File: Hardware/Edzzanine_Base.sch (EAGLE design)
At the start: 39 parts, among them U1 MIC5219 3.3V, U2 FTS31XS-U

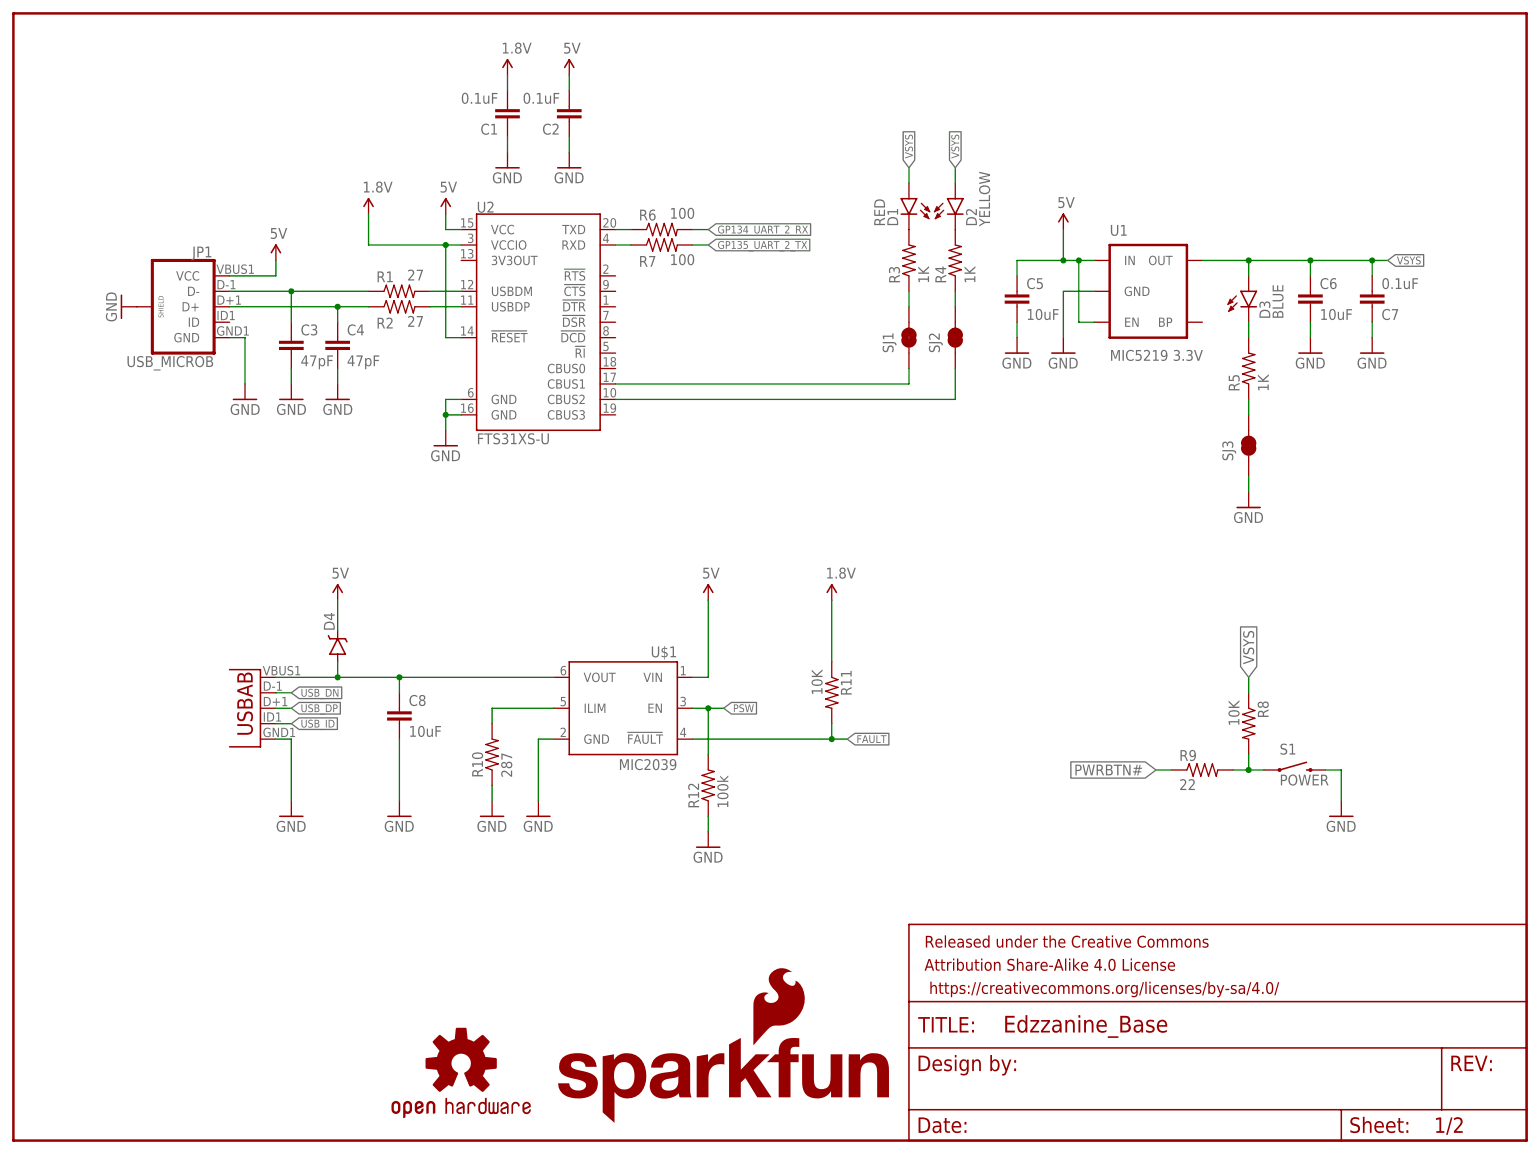
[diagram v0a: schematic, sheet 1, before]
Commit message: changed out power supply for something more powerful. Added fiducials
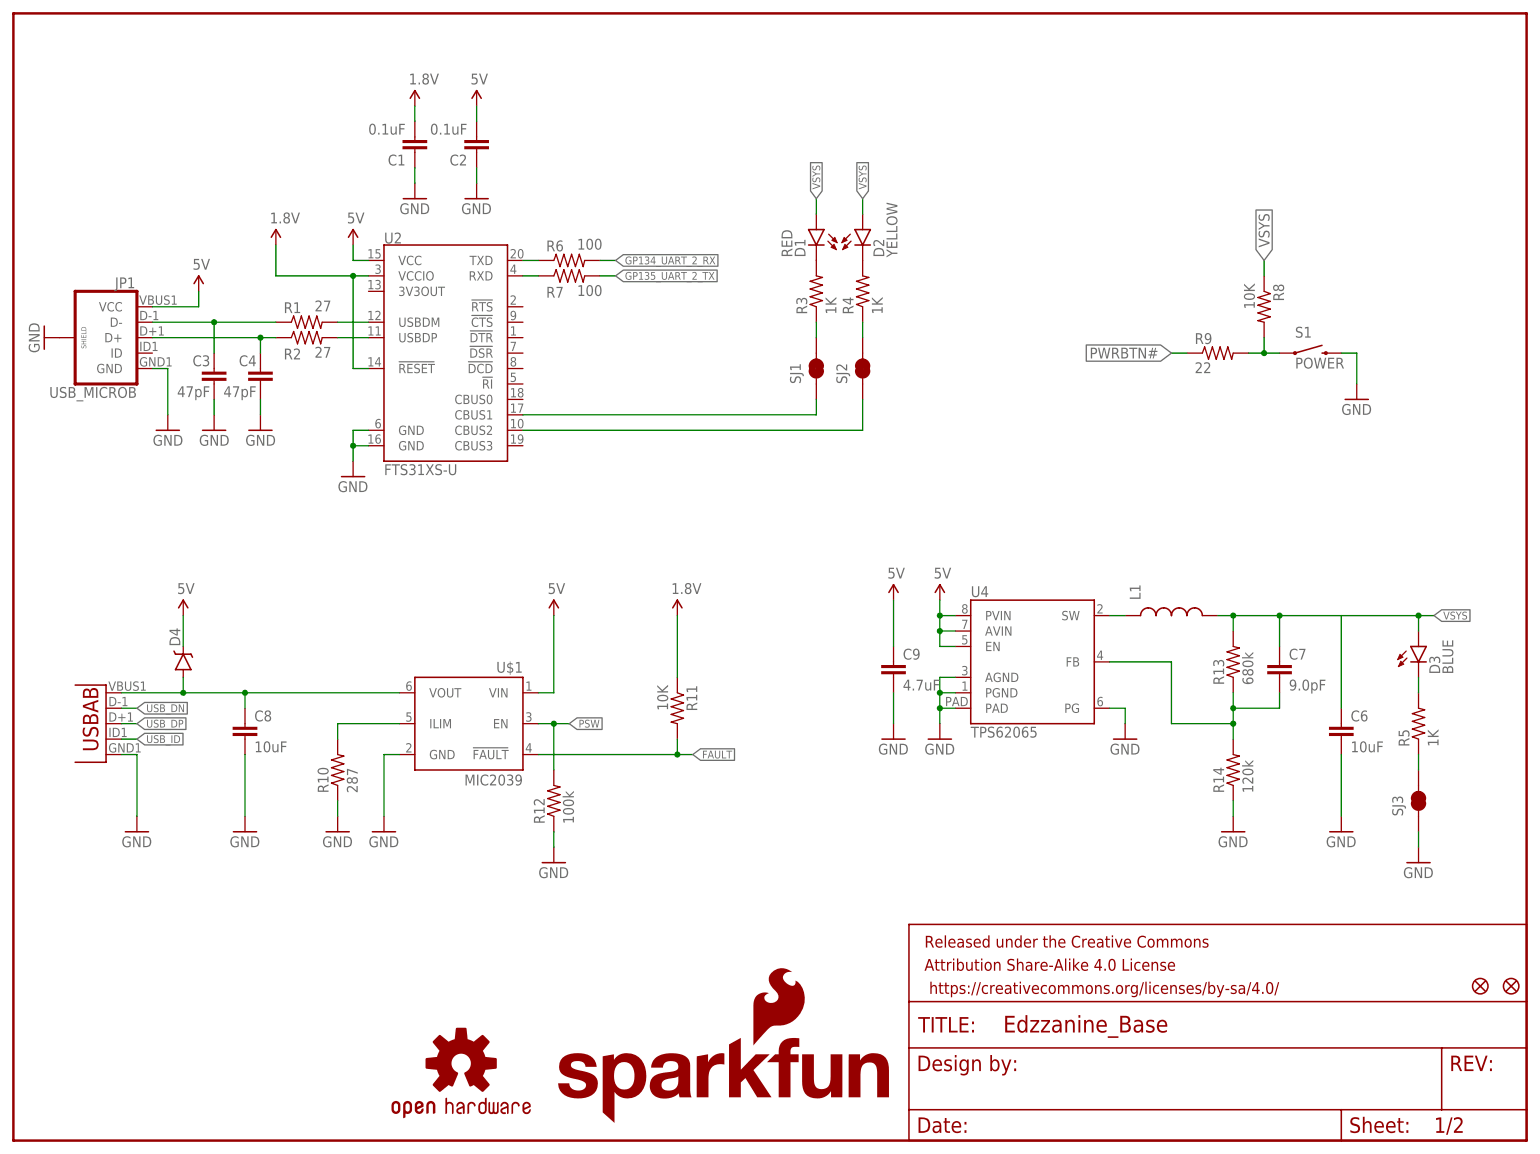
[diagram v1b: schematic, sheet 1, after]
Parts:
- removed C5: 10uF, SparkFun-Capacitors:10UF-6.3V-20%(1206)
- removed U1: MIC5219 3.3V, SparkFun-PowerIC:V_REG_MIC52193.3V
- added C9: 4.7uF, SparkFun-Capacitors:4.7UF-6.3V-10%(0603)0603
- added FID1, FID2: FIDUCIAL1X2, SparkFun-Aesthetics:FIDUCIAL1X2
- added L1: (no value), SparkFun-Passives:INDUCTOR
- added R13: 680k, SparkFun-Resistors:RESISTOR0603
- added R14: 120k, SparkFun-Resistors:RESISTOR0603
- added U4: TPS62065, Testing:TPS62065
- C7: value 0.1uF -> 9.0pF; device SparkFun-Capacitors:0.1UF-25V-5%(0603) -> SparkFun-Capacitors:9.0PF-50V-10%(0603)
- renumbered LOGO2 to LOGO4, LOGO3 to LOGO1
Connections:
- new net N$17: C7.2, R13.1, R14.2, U4.FB
- new net N$19: L1.1, U4.SW
- net 5V: now also C9.1, U4.AVIN, U4.EN, U4.PVIN; no longer C5.1, U1.EN, U1.IN
- net GND: now also C9.2, R14.1, U4.AGND, U4.PAD, U4.PG, U4.PGND; no longer C5.2, C7.1, U1.GND
- net VSYS: now also C7.1, L1.2, R13.2; no longer C7.2, U1.OUT
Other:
- moved on the sheet: C1, C2, C3, C4, C6, C7, C8, D1, D2, D3, D4, JP1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

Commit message: Corrected OTG power issue Corrected name and position added DCIN pin to connector Added DCIN enable circuit corrected dimensions and cleaned up drawings replaced power button with new SMD side shooting button.
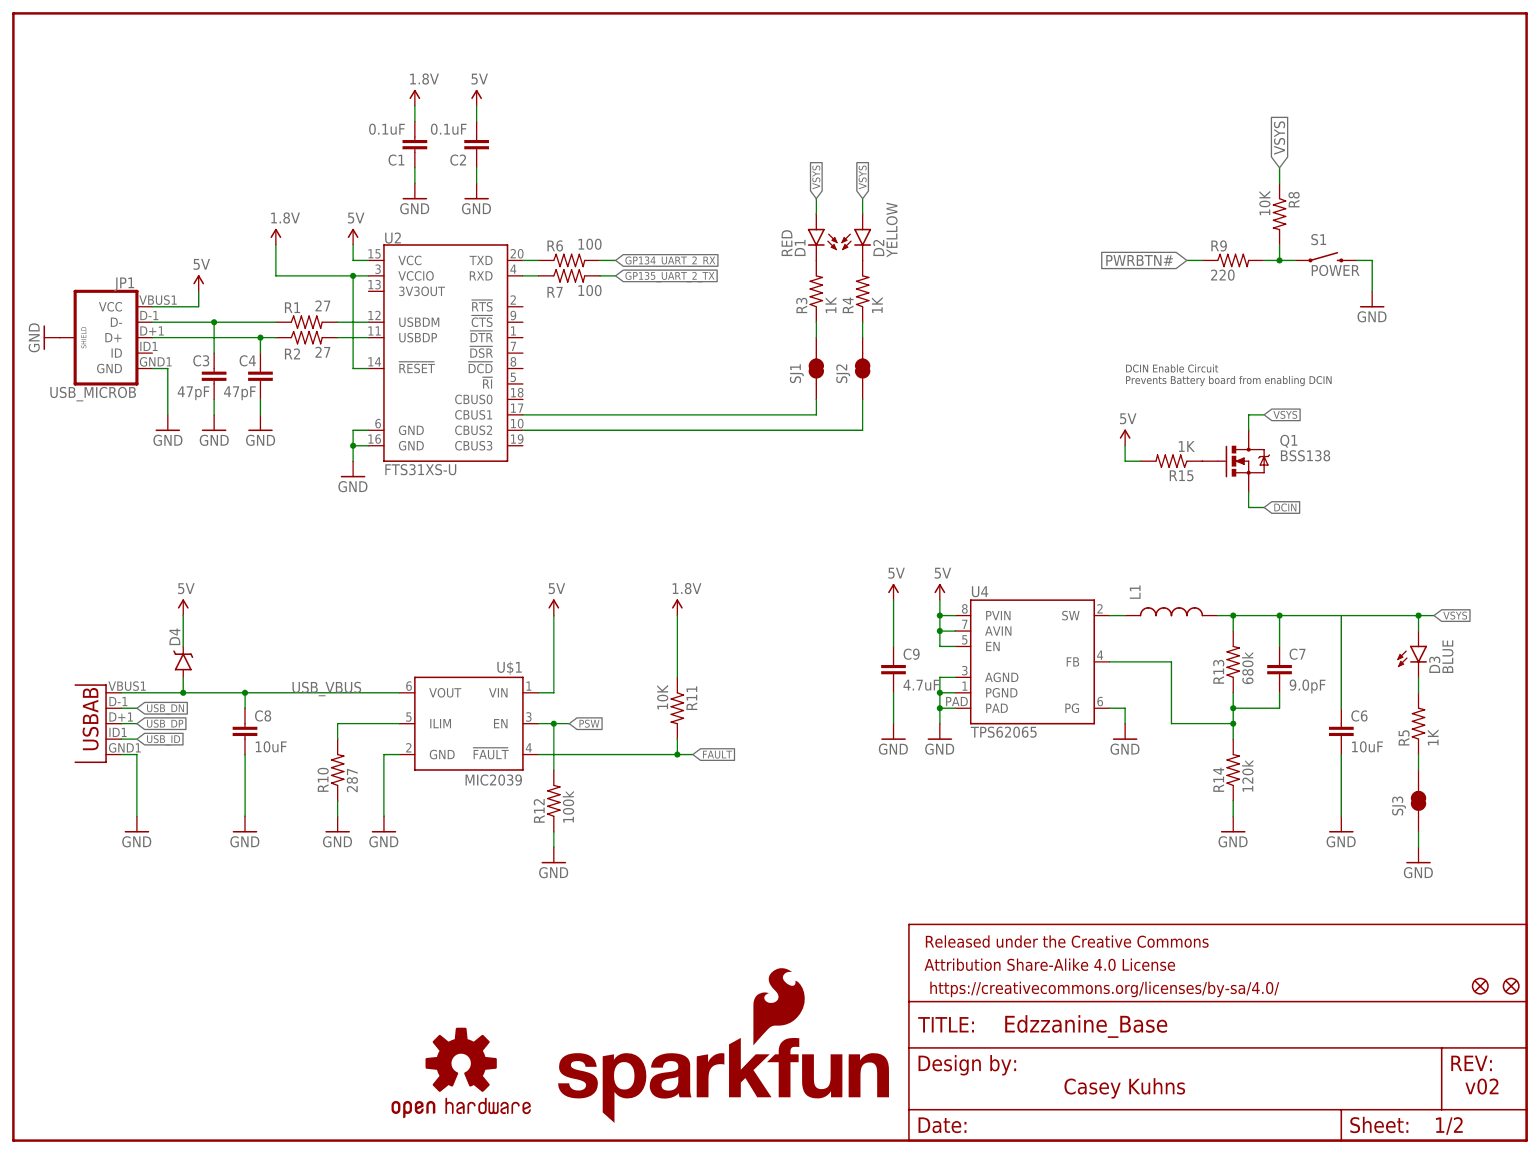
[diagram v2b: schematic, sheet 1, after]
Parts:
- added Q1: BSS138, SparkFun-DiscreteSemi:MOSFET-NCHANNELBSS138
- added R15: 1K, SparkFun-Resistors:1KOHM1/10W1%(0603)
- C1, C2: device SparkFun-Capacitors:0.1UF-25V-5%(0603) -> SparkFun-Capacitors:0.1UF-25V(+80/-20%)(0603)
- R9: value 22 -> 220
- S1: device SparkFun-Electromechanical:SWITCH-MOMENTARY-2-SMD-1101NE -> SparkFun-Electromechanical:SWITCH-MOMENTARY-2TACTILE-SWITCH-SMD-RIGHT-ANGLE
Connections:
- new net DCIN: E1.DCIN, Q1.S, U$3.DCIN
- net 5V: now also R15.2
- net N$18: now also Q1.G, R15.1; no longer C8.1, D4.A, U$1.VOUT, U3.VBUS
- net USB_VBUS: now also C8.1, D4.A, U$1.VOUT, U3.VBUS
- net VSYS: now also Q1.D
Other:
- note added: "Casey Kuhns"
- note added: "DCIN Enable Circuit Prevents Battery board from enabling DCIN"
- note added: "v02"
- moved on the sheet: R8, R9, S1
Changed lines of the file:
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@@
 <part name="GND5" library="SparkFun-Aesthetics" deviceset="GND" device=""/>
 <part name="U2" library="SparkFun-DigitalIC" deviceset="FT231X" device="S" value="FTS31XS-U"/>
-<part name="C1" library="SparkFun-Capacitors" deviceset="0.1UF-25V-5%(0603)" device="" value="0.1uF"/>
-<part name="C2" library="SparkFun-Capacitors" deviceset="0.1UF-25V-5%(0603)" device="" value="0.1uF"/>
+<part name="C1" library="SparkFun-Capacitors" deviceset="0.1UF-25V(+80/-20%)(0603)" device="" value="0.1uF"/>
+<part name="C2" library="SparkFun-Capacitors" deviceset="0.1UF-25V(+80/-20%)(0603)" device="" value="0.1uF"/>
 <part name="GND2" library="SparkFun-Aesthetics" deviceset="GND" device=""/>
 <part name="GND6" library="SparkFun-Aesthetics" deviceset="GND" device=""/>
@@
 <part name="R6" library="SparkFun-Resistors" deviceset="100OHM1/10W1%(0603)" device="" value="100"/>
 <part name="R7" library="SparkFun-Resistors" deviceset="100OHM1/10W1%(0603)" device="" value="100"/>
-<part name="S1" library="SparkFun-Electromechanical" deviceset="SWITCH-MOMENTARY-2" device="-SMD-1101NE" value="POWER"/>
+<part name="S1" library="SparkFun-Electromechanical" deviceset="SWITCH-MOMENTARY-2" device="TACTILE-SWITCH-SMD-RIGHT-ANGLE" value="POWER"/>
 <part name="R8" library="SparkFun-Resistors" deviceset="10KOHM1/10W1%(0603)" device="0603" value="10K"/>
-<part name="R9" library="SparkFun-Resistors" deviceset="22OHM1/10W1%(0603)" device="" value="22"/>
+<part name="R9" library="SparkFun-Resistors" deviceset="22OHM1/10W1%(0603)" device="" value="220"/>
 <part name="GND15" library="SparkFun-Aesthetics" deviceset="GND" device=""/>
 <part name="U3" library="SparkFun-Connectors" deviceset="USB-AB" device="CONN-11794"/>
@@
 <part name="FID1" library="SparkFun-Aesthetics" deviceset="FIDUCIAL" device="1X2"/>
 <part name="FID2" library="SparkFun-Aesthetics" deviceset="FIDUCIAL" device="1X2"/>
+<part name="Q1" library="SparkFun-DiscreteSemi" deviceset="MOSFET-NCHANNEL" device="BSS138" value="BSS138"/>
+<part name="R15" library="SparkFun-Resistors" deviceset="1KOHM1/10W1%(0603)" device="" value="1K"/>
+<part name="SUPPLY7" library="SparkFun-Aesthetics" deviceset="5V" device=""/>
 </parts>
 <sheets>
 <sheet>
 <plain>
+<text x="182.88" y="124.46" size="1.27" layer="97">DCIN Enable Circuit
+Prevents Battery board from enabling DCIN</text>
+<text x="172.72" y="7.62" size="2.54" layer="94">Casey Kuhns</text>
+<text x="238.76" y="7.62" size="2.54" layer="94">v02</text>
 </plain>
 <instances>
@@
 <attribute name="VALUE" x="92.71" y="138.938" size="1.778" layer="96"/>
 </instance>
-<instance part="S1" gate="G$1" x="213.36" y="129.54"/>
-<instance part="R8" gate="G$1" x="205.74" y="137.16" rot="R270"/>
-<instance part="R9" gate="G$1" x="198.12" y="129.54"/>
-<instance part="GND15" gate="1" x="220.98" y="121.92"/>
+<instance part="S1" gate="G$1" x="215.9" y="144.78"/>
+<instance part="R8" gate="G$1" x="208.28" y="152.4" rot="R270"/>
+<instance part="R9" gate="G$1" x="200.66" y="144.78"/>
+<instance part="GND15" gate="1" x="223.52" y="137.16"/>
 <instance part="U3" gate="G$1" x="12.7" y="68.58" rot="R180"/>
 <instance part="GND16" gate="1" x="20.32" y="50.8"/>
@@
 <instance part="FID1" gate="G$1" x="246.38" y="25.4"/>
 <instance part="FID2" gate="G$1" x="241.3" y="25.4"/>
+<instance part="Q1" gate="G$1" x="203.2" y="111.76"/>
+<instance part="R15" gate="G$1" x="190.5" y="111.76" rot="R180"/>
+<instance part="SUPPLY7" gate="G$1" x="182.88" y="114.3"/>
 </instances>
 <busses>
@@
 <segment>
 <pinref part="S1" gate="G$1" pin="2"/>
-<wire x1="218.44" y1="129.54" x2="220.98" y2="129.54" width="0.1524" layer="91"/>
-<wire x1="220.98" y1="129.54" x2="220.98" y2="124.46" width="0.1524" layer="91"/>
+<wire x1="220.98" y1="144.78" x2="223.52" y2="144.78" width="0.1524" layer="91"/>
+<wire x1="223.52" y1="144.78" x2="223.52" y2="139.7" width="0.1524" layer="91"/>
 <pinref part="GND15" gate="1" pin="GND"/>
 </segment>
@@
 <pinref part="SUPPLY11" gate="G$1" pin="5V"/>
 <pinref part="C9" gate="G$1" pin="1"/>
+</segment>
+<segment>
+<pinref part="R15" gate="G$1" pin="2"/>
+<wire x1="182.88" y1="111.76" x2="185.42" y2="111.76" width="0.1524" layer="91"/>
+<pinref part="SUPPLY7" gate="G$1" pin="5V"/>
+<wire x1="182.88" y1="111.76" x2="182.88" y2="114.3" width="0.1524" layer="91"/>
 </segment>
 </net>
@@
 </segment>
 <segment>
-<wire x1="205.74" y1="142.24" x2="205.74" y2="144.78" width="0.1524" layer="91"/>
+<wire x1="208.28" y1="157.48" x2="208.28" y2="160.02" width="0.1524" layer="91"/>
 <pinref part="R8" gate="G$1" pin="1"/>
-<label x="205.74" y="144.78" size="1.778" layer="95" rot="R90" xref="yes"/>
+<label x="208.28" y="160.02" size="1.778" layer="95" rot="R90" xref="yes"/>
+</segment>
+<segment>
+<pinref part="Q1" gate="G$1" pin="D"/>
+<wire x1="203.2" y1="116.84" x2="203.2" y2="119.38" width="0.1524" layer="91"/>
+<wire x1="203.2" y1="119.38" x2="205.74" y2="119.38" width="0.1524" layer="91"/>
+<label x="205.74" y="119.38" size="1.27" layer="95" xref="yes"/>
 </segment>
 </net>
@@
 <pinref part="R9" gate="G$1" pin="2"/>
 <pinref part="R8" gate="G$1" pin="2"/>
-<wire x1="203.2" y1="129.54" x2="205.74" y2="129.54" width="0.1524" layer="91"/>
-<wire x1="205.74" y1="129.54" x2="205.74" y2="132.08" width="0.1524" layer="91"/>
+<wire x1="205.74" y1="144.78" x2="208.28" y2="144.78" width="0.1524" layer="91"/>
+<wire x1="208.28" y1="144.78" x2="208.28" y2="147.32" width="0.1524" layer="91"/>
 <pinref part="S1" gate="G$1" pin="1"/>
-<wire x1="205.74" y1="129.54" x2="208.28" y2="129.54" width="0.1524" layer="91"/>
-<junction x="205.74" y="129.54"/>
+<wire x1="208.28" y1="144.78" x2="210.82" y2="144.78" width="0.1524" layer="91"/>
+<junction x="208.28" y="144.78"/>
 </segment>
 </net>
@@
 <segment>
 <pinref part="R9" gate="G$1" pin="1"/>
-<wire x1="193.04" y1="129.54" x2="190.5" y2="129.54" width="0.1524" layer="91"/>
-<label x="190.5" y="129.54" size="1.778" layer="95" rot="R180" xref="yes"/>
+<wire x1="195.58" y1="144.78" x2="193.04" y2="144.78" width="0.1524" layer="91"/>
+<label x="193.04" y="144.78" size="1.778" layer="95" rot="R180" xref="yes"/>
 </segment>
 </net>
@@
 </segment>
 </net>
-<net name="N$18" class="0">
+<net name="USB_VBUS" class="0">
 <segment>
 <pinref part="U3" gate="G$1" pin="VBUS"/>
@@
 <wire x1="38.1" y1="73.66" x2="63.5" y2="73.66" width="0.1524" layer="91"/>
 <junction x="38.1" y="73.66"/>
+<label x="45.72" y="73.66" size="1.778" layer="95"/>
 </segment>
 </net>
@@
 <pinref part="L1" gate="G$1" pin="1"/>
 <wire x1="182.88" y1="86.36" x2="180.34" y2="86.36" width="0.1524" layer="91"/>
+</segment>
+</net>
+<net name="DCIN" class="0">
+<segment>
+<wire x1="203.2" y1="104.14" x2="205.74" y2="104.14" width="0.1524" layer="91"/>
+<label x="205.74" y="104.14" size="1.27" layer="95" xref="yes"/>
+<pinref part="Q1" gate="G$1" pin="S"/>
+<wire x1="203.2" y1="104.14" x2="203.2" y2="106.68" width="0.1524" layer="91"/>
+</segment>
+</net>
+<net name="N$18" class="0">
+<segment>
+<pinref part="Q1" gate="G$1" pin="G"/>
+<pinref part="R15" gate="G$1" pin="1"/>
 </segment>
 </net>
@@
 </segment>
 </net>
+<net name="DCIN" class="0">
+<segment>
+<pinref part="U$3" gate="G$1" pin="DCIN"/>
+<wire x1="172.72" y1="152.4" x2="170.18" y2="152.4" width="0.1524" layer="91"/>
+<label x="170.18" y="152.4" size="1.27" layer="95" rot="R180" xref="yes"/>
+</segment>
+<segment>
+<pinref part="E1" gate="G$1" pin="DCIN"/>
+<wire x1="25.4" y1="152.4" x2="22.86" y2="152.4" width="0.1524" layer="91"/>
+<label x="22.86" y="152.4" size="1.27" layer="95" rot="R180" xref="yes"/>
+</segment>
+</net>
 </nets>
 </sheet>
@@
 </schematic>
 </drawing>
+<compatibility>
+<note version="6.3" minversion="6.2.2" severity="warning">
+Since Version 6.2.2 text objects can contain more than one line,
+which will not be processed correctly with this version.
+</note>
+</compatibility>
 </eagle>
